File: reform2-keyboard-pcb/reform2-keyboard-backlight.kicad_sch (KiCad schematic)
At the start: 31 parts, among them J100 Conn_01x03, J5 Conn_01x03

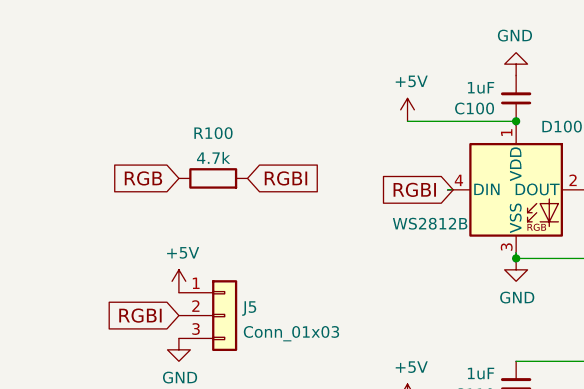
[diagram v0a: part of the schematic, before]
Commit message: more routing of smd parts, add sockets
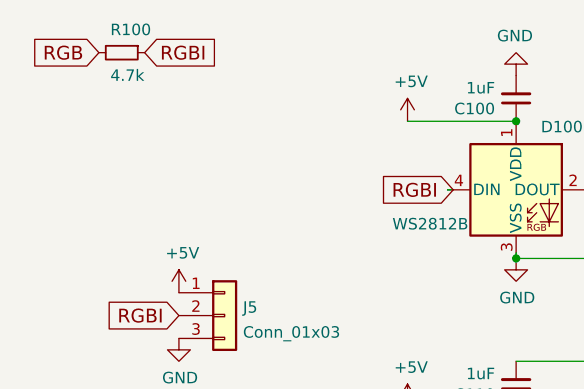
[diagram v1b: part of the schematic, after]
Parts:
- removed R100: 4.7k, Resistor_SMD:R_0603_1608Metric, symbol Device:R
- added R100: 4.7k, Resistor_SMD:R_0603_1608Metric, symbol reform2-keyboard-rescue:R_Small-Device
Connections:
- net RGB: now also R100.2
- net RGBI: now also R100.1
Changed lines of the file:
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@@
     )
   )
-  (global_label "RGBI" (shape input) (at 48.26 40.005 0) (fields_autoplaced)
+  (global_label "RGBI" (shape input) (at 36.83 26.035 0) (fields_autoplaced)
     (effects (font (size 1.524 1.524)) (justify left))
-    (property "Intersheet References" "${INTERSHEET_REFS}" (id 0) (at 56.3466 40.1002 0)
+    (property "Intersheet References" "${INTERSHEET_REFS}" (id 0) (at 44.9166 26.1302 0)
       (effects (font (size 1.524 1.524)) (justify left) hide)
     )
@@
     )
   )
-  (global_label "RGB" (shape input) (at 40.64 40.005 180) (fields_autoplaced)
+  (global_label "RGB" (shape input) (at 31.75 26.035 180) (fields_autoplaced)
     (effects (font (size 1.524 1.524)) (justify right))
-    (property "Intersheet References" "${INTERSHEET_REFS}" (id 0) (at 33.2791 39.9098 0)
+    (property "Intersheet References" "${INTERSHEET_REFS}" (id 0) (at 24.3891 25.9398 0)
       (effects (font (size 1.524 1.524)) (justify right) hide)
     )
@@
     (pin "1")
   )
+  (symbol (lib_id "reform2-keyboard-rescue:R_Small-Device") (at 34.29 26.035 270) (unit 1)
+    (in_bom yes) (on_board yes)
+    (property "Reference" "R100" (id 0) (at 33.02 23.495 90)
+      (effects (font (size 1.27 1.27)) (justify left))
+    )
+    (property "Value" "4.7k" (id 1) (at 33.02 28.575 90)
+      (effects (font (size 1.27 1.27)) (justify left))
+    )
+    (property "Footprint" "Resistor_SMD:R_0603_1608Metric" (id 2) (at 34.29 26.035 0)
+      (effects (font (size 1.27 1.27)) hide)
+    )
+    (property "Datasheet" "" (id 3) (at 34.29 26.035 0)
+      (effects (font (size 1.27 1.27)) hide)
+    )
+    (property "Manufacturer" "Vishay Dale" (id 4) (at 34.29 26.035 0)
+      (effects (font (size 1.27 1.27)) hide)
+    )
+    (property "Manufacturer_No" "CRCW06030000Z0EAC" (id 5) (at 34.29 26.035 0)
+      (effects (font (size 1.27 1.27)) hide)
+    )
+    (pin "1")
+    (pin "2")
+  )
   (symbol (lib_id "power:GND") (at 198.755 80.645 0) (unit 1)
     (in_bom yes) (on_board yes)
@@
     (pin "1")
   )
-  (symbol (lib_id "Device:R") (at 44.45 40.005 90) (unit 1)
-    (in_bom yes) (on_board yes) (fields_autoplaced)
-    (property "Reference" "R100" (id 0) (at 44.45 35.0225 90))
-    (property "Value" "4.7k" (id 1) (at 44.45 37.7976 90))
-    (property "Footprint" "Resistor_SMD:R_0603_1608Metric" (id 2) (at 44.45 41.783 90)
-      (effects (font (size 1.27 1.27)) hide)
-    )
-    (property "Datasheet" "~" (id 3) (at 44.45 40.005 0)
-      (effects (font (size 1.27 1.27)) hide)
-    )
-    (pin "1")
-    (pin "2")
-  )
   (symbol (lib_id "reform2-keyboard-rescue:C_Small-Device") (at 150.495 31.115 180) (unit 1)

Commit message: change parts for better handsolders
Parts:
- R100: footprint Resistor_SMD:R_0603_1608Metric -> Resistor_SMD:R_0805_2012Metric_Pad1.20x1.40mm_HandSolder
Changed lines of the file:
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@@
       (effects (font (size 1.27 1.27)) (justify left))
     )
-    (property "Footprint" "Resistor_SMD:R_0603_1608Metric" (id 2) (at 34.29 26.035 0)
+    (property "Footprint" "Resistor_SMD:R_0805_2012Metric_Pad1.20x1.40mm_HandSolder" (id 2) (at 34.29 26.035 0)
       (effects (font (size 1.27 1.27)) hide)
     )

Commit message: flip caps for RGB leds
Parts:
- C100, C101, C102, C103, C104, C105, C106, C110, C111, C112, C113, C114, C115, C116: footprint Capacitor_SMD:C_0603_1608Metric -> Capacitor_SMD:C_0805_2012Metric_Pad1.18x1.45mm_HandSolder
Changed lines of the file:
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@@
       (effects (font (size 1.27 1.27)) (justify left))
     )
-    (property "Footprint" "Capacitor_SMD:C_0603_1608Metric" (id 2) (at 78.105 31.115 0)
+    (property "Footprint" "Capacitor_SMD:C_0805_2012Metric_Pad1.18x1.45mm_HandSolder" (id 2) (at 78.105 31.115 0)
       (effects (font (size 1.27 1.27)) hide)
     )
@@
       (effects (font (size 1.27 1.27)) (justify left))
     )
-    (property "Footprint" "Capacitor_SMD:C_0603_1608Metric" (id 2) (at 150.495 62.865 0)
+    (property "Footprint" "Capacitor_SMD:C_0805_2012Metric_Pad1.18x1.45mm_HandSolder" (id 2) (at 150.495 62.865 0)
       (effects (font (size 1.27 1.27)) hide)
     )
@@
       (effects (font (size 1.27 1.27)) (justify left))
     )
-    (property "Footprint" "Capacitor_SMD:C_0603_1608Metric" (id 2) (at 222.885 31.115 0)
+    (property "Footprint" "Capacitor_SMD:C_0805_2012Metric_Pad1.18x1.45mm_HandSolder" (id 2) (at 222.885 31.115 0)
       (effects (font (size 1.27 1.27)) hide)
     )
@@
       (effects (font (size 1.27 1.27)) (justify left))
     )
-    (property "Footprint" "Capacitor_SMD:C_0603_1608Metric" (id 2) (at 174.625 62.865 0)
+    (property "Footprint" "Capacitor_SMD:C_0805_2012Metric_Pad1.18x1.45mm_HandSolder" (id 2) (at 174.625 62.865 0)
       (effects (font (size 1.27 1.27)) hide)
     )
@@
       (effects (font (size 1.27 1.27)) (justify left))
     )
-    (property "Footprint" "Capacitor_SMD:C_0603_1608Metric" (id 2) (at 102.235 31.115 0)
+    (property "Footprint" "Capacitor_SMD:C_0805_2012Metric_Pad1.18x1.45mm_HandSolder" (id 2) (at 102.235 31.115 0)
       (effects (font (size 1.27 1.27)) hide)
     )
@@
       (effects (font (size 1.27 1.27)) (justify left))
     )
-    (property "Footprint" "Capacitor_SMD:C_0603_1608Metric" (id 2) (at 198.755 62.865 0)
+    (property "Footprint" "Capacitor_SMD:C_0805_2012Metric_Pad1.18x1.45mm_HandSolder" (id 2) (at 198.755 62.865 0)
       (effects (font (size 1.27 1.27)) hide)
     )
@@
       (effects (font (size 1.27 1.27)) (justify left))
     )
-    (property "Footprint" "Capacitor_SMD:C_0603_1608Metric" (id 2) (at 78.105 62.865 0)
+    (property "Footprint" "Capacitor_SMD:C_0805_2012Metric_Pad1.18x1.45mm_HandSolder" (id 2) (at 78.105 62.865 0)
       (effects (font (size 1.27 1.27)) hide)
     )
@@
       (effects (font (size 1.27 1.27)) (justify left))
     )
-    (property "Footprint" "Capacitor_SMD:C_0603_1608Metric" (id 2) (at 174.625 31.115 0)
+    (property "Footprint" "Capacitor_SMD:C_0805_2012Metric_Pad1.18x1.45mm_HandSolder" (id 2) (at 174.625 31.115 0)
       (effects (font (size 1.27 1.27)) hide)
     )
@@
       (effects (font (size 1.27 1.27)) (justify left))
     )
-    (property "Footprint" "Capacitor_SMD:C_0603_1608Metric" (id 2) (at 222.885 62.865 0)
+    (property "Footprint" "Capacitor_SMD:C_0805_2012Metric_Pad1.18x1.45mm_HandSolder" (id 2) (at 222.885 62.865 0)
       (effects (font (size 1.27 1.27)) hide)
     )
@@
       (effects (font (size 1.27 1.27)) (justify left))
     )
-    (property "Footprint" "Capacitor_SMD:C_0603_1608Metric" (id 2) (at 150.495 31.115 0)
+    (property "Footprint" "Capacitor_SMD:C_0805_2012Metric_Pad1.18x1.45mm_HandSolder" (id 2) (at 150.495 31.115 0)
       (effects (font (size 1.27 1.27)) hide)
     )
@@
       (effects (font (size 1.27 1.27)) (justify left))
     )
-    (property "Footprint" "Capacitor_SMD:C_0603_1608Metric" (id 2) (at 198.755 31.115 0)
+    (property "Footprint" "Capacitor_SMD:C_0805_2012Metric_Pad1.18x1.45mm_HandSolder" (id 2) (at 198.755 31.115 0)
       (effects (font (size 1.27 1.27)) hide)
     )
@@
       (effects (font (size 1.27 1.27)) (justify left))
     )
-    (property "Footprint" "Capacitor_SMD:C_0603_1608Metric" (id 2) (at 126.365 31.115 0)
+    (property "Footprint" "Capacitor_SMD:C_0805_2012Metric_Pad1.18x1.45mm_HandSolder" (id 2) (at 126.365 31.115 0)
       (effects (font (size 1.27 1.27)) hide)
     )
@@
       (effects (font (size 1.27 1.27)) (justify left))
     )
-    (property "Footprint" "Capacitor_SMD:C_0603_1608Metric" (id 2) (at 102.235 62.865 0)
+    (property "Footprint" "Capacitor_SMD:C_0805_2012Metric_Pad1.18x1.45mm_HandSolder" (id 2) (at 102.235 62.865 0)
       (effects (font (size 1.27 1.27)) hide)
     )
@@
       (effects (font (size 1.27 1.27)) (justify left))
     )
-    (property "Footprint" "Capacitor_SMD:C_0603_1608Metric" (id 2) (at 126.365 62.865 0)
-      (effects (font (size 1.27 1.27)) hide)
-    )
+    (property "Footprint" "Capacitor_SMD:C_0805_2012Metric_Pad1.18x1.45mm_HandSolder" (id 2) (at 126.365 62.865 0)
+      (effects (font (size 1.27 1.27)) hide)
+    )

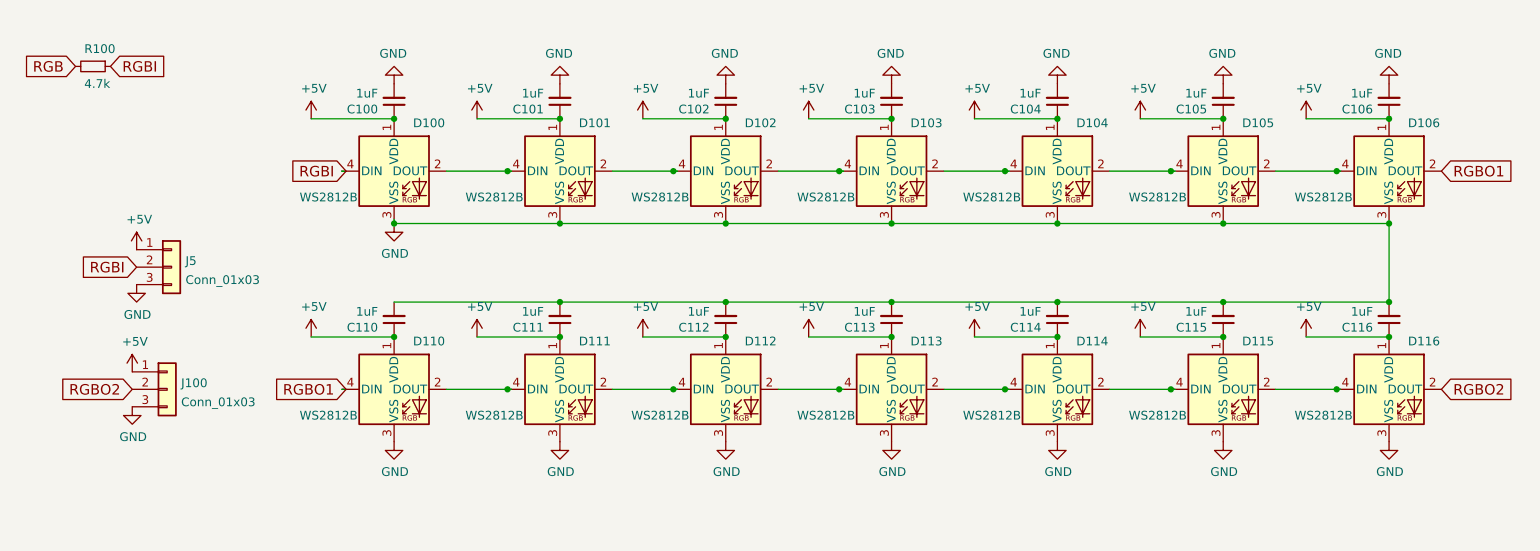
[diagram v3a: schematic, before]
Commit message: added testpoints for RGB, fixed diode directions, started BOM & top POS for assembly
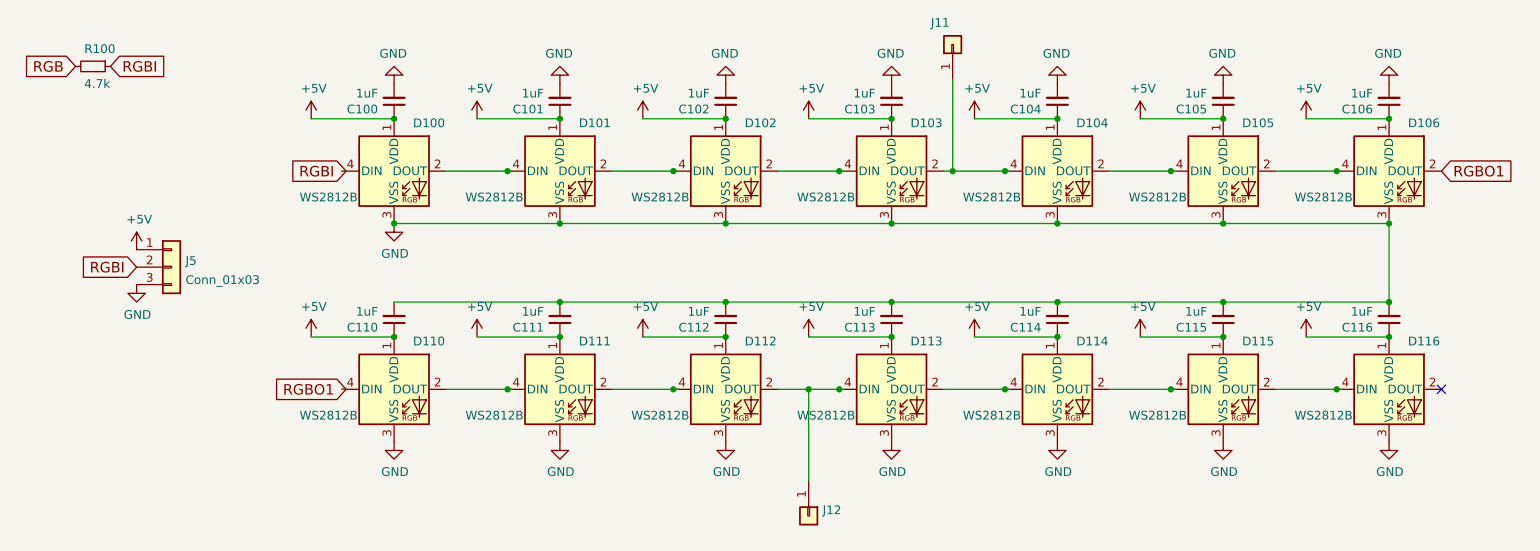
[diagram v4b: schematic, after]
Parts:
- removed J100: Conn_01x03, Connector_PinHeader_2.54mm:PinHeader_1x03_P2.54mm_Vertical, symbol Connector_Generic:Conn_01x03
- added J11, J12: (no value), symbol Connector_Generic:Conn_01x01
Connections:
- net at D103.2 (DOUT), D104.4 (DIN): now also J11.1 (Pin_1)
- net at D112.2 (DOUT), D113.4 (DIN): now also J12.1 (Pin_1)
- net RGBO2: no longer names the net of D116.2 (DOUT)
- no-connect marks 0 -> 1
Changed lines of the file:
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@@
   (junction (at 198.755 60.325) (diameter 0) (color 0 0 0 0)
   )
+  (junction (at 138.43 73.025) (diameter 0) (color 0 0 0 0)
+  )
   (junction (at 150.495 60.325) (diameter 0) (color 0 0 0 0)
   )
   (junction (at 94.615 73.025) (diameter 0) (color 0 0 0 0)
   )
+  (junction (at 159.385 41.275) (diameter 0) (color 0 0 0 0)
+  )
   (junction (at 150.495 48.895) (diameter 0) (color 0 0 0 0)
   )
@@
   (junction (at 198.755 33.655) (diameter 0) (color 0 0 0 0)
   )
+  (no_connect (at 230.505 73.025))
   (wire (pts (xy 198.755 60.325) (xy 222.885 60.325))
     (stroke (width 0) (type default) (color 0 0 0 0))
@@
     (stroke (width 0) (type default) (color 0 0 0 0))
   )
-  (wire (pts (xy 158.115 41.275) (xy 167.005 41.275))
+  (wire (pts (xy 158.115 41.275) (xy 159.385 41.275))
     (stroke (width 0) (type default) (color 0 0 0 0))
   )
@@
     (stroke (width 0) (type default) (color 0 0 0 0))
   )
+  (wire (pts (xy 159.385 41.275) (xy 167.005 41.275))
+    (stroke (width 0) (type default) (color 0 0 0 0))
+  )
   (wire (pts (xy 102.235 48.895) (xy 78.105 48.895))
     (stroke (width 0) (type default) (color 0 0 0 0))
@@
     (stroke (width 0) (type default) (color 0 0 0 0))
   )
-  (wire (pts (xy 133.985 73.025) (xy 142.875 73.025))
+  (wire (pts (xy 133.985 73.025) (xy 138.43 73.025))
     (stroke (width 0) (type default) (color 0 0 0 0))
   )
@@
     (stroke (width 0) (type default) (color 0 0 0 0))
   )
+  (wire (pts (xy 138.43 73.025) (xy 142.875 73.025))
+    (stroke (width 0) (type default) (color 0 0 0 0))
+  )
   (wire (pts (xy 206.375 41.275) (xy 215.265 41.275))
     (stroke (width 0) (type default) (color 0 0 0 0))
@@
     (stroke (width 0) (type default) (color 0 0 0 0))
   )
+  (wire (pts (xy 138.43 86.36) (xy 138.43 73.025))
+    (stroke (width 0) (type default) (color 0 0 0 0))
+  )
   (wire (pts (xy 162.56 33.655) (xy 174.625 33.655))
     (stroke (width 0) (type default) (color 0 0 0 0))
@@
   )
   (wire (pts (xy 186.69 33.655) (xy 198.755 33.655))
+    (stroke (width 0) (type default) (color 0 0 0 0))
+  )
+  (wire (pts (xy 159.385 27.94) (xy 159.385 41.275))
     (stroke (width 0) (type default) (color 0 0 0 0))
   )
@@
     )
   )
-  (global_label "RGBO2" (shape input) (at 230.505 73.025 0) (fields_autoplaced)
-    (effects (font (size 1.524 1.524)) (justify left))
-    (property "Intersheet References" "${INTERSHEET_REFS}" (id 0) (at 240.9139 72.9298 0)
-      (effects (font (size 1.524 1.524)) (justify left) hide)
-    )
-  )
-  (global_label "RGBO2" (shape input) (at 40.005 73.025 180) (fields_autoplaced)
-    (effects (font (size 1.524 1.524)) (justify right))
-    (property "Intersheet References" "${INTERSHEET_REFS}" (id 0) (at 29.5961 72.9298 0)
-      (effects (font (size 1.524 1.524)) (justify right) hide)
-    )
-  )
   (global_label "RGB" (shape input) (at 31.75 26.035 180) (fields_autoplaced)
     (effects (font (size 1.524 1.524)) (justify right))
@@
     (pin "1")
   )
-  (symbol (lib_id "power:GND") (at 40.005 75.565 0) (unit 1)
-    (in_bom yes) (on_board yes)
-    (property "Reference" "#PWR0112" (id 0) (at 40.005 81.915 0)
-      (effects (font (size 1.27 1.27)) hide)
-    )
-    (property "Value" "GND" (id 1) (at 40.132 79.9592 0))
-    (property "Footprint" "" (id 2) (at 40.005 75.565 0)
-      (effects (font (size 1.27 1.27)) hide)
-    )
-    (property "Datasheet" "" (id 3) (at 40.005 75.565 0)
+  (symbol (lib_id "Connector_Generic:Conn_01x01") (at 159.385 22.86 90) (unit 1)
+    (in_bom yes) (on_board yes)
+    (property "Reference" "J11" (id 0) (at 156.21 19.685 90)
+      (effects (font (size 1.27 1.27)) (justify right))
+    )
+    (property "Value" "" (id 1) (at 160.655 19.685 90)
+      (effects (font (size 1.27 1.27)) (justify right))
+    )
+    (property "Footprint" "" (id 2) (at 159.385 22.86 0)
+      (effects (font (size 1.27 1.27)) hide)
+    )
+    (property "Datasheet" "~" (id 3) (at 159.385 22.86 0)
       (effects (font (size 1.27 1.27)) hide)
     )
@@
     (pin "1")
   )
-  (symbol (lib_id "Connector_Generic:Conn_01x03") (at 45.085 73.025 0) (unit 1)
-    (in_bom yes) (on_board yes) (fields_autoplaced)
-    (property "Reference" "J100" (id 0) (at 47.117 72.1165 0)
-      (effects (font (size 1.27 1.27)) (justify left))
-    )
-    (property "Value" "Conn_01x03" (id 1) (at 47.117 74.8916 0)
-      (effects (font (size 1.27 1.27)) (justify left))
-    )
-    (property "Footprint" "Connector_PinHeader_2.54mm:PinHeader_1x03_P2.54mm_Vertical" (id 2) (at 45.085 73.025 0)
-      (effects (font (size 1.27 1.27)) hide)
-    )
-    (property "Datasheet" "~" (id 3) (at 45.085 73.025 0)
-      (effects (font (size 1.27 1.27)) hide)
-    )
-    (pin "1")
-    (pin "2")
-    (pin "3")
-  )
   (symbol (lib_id "power:+5V") (at 114.3 33.655 0) (unit 1)
     (in_bom yes) (on_board yes)
@@
     (pin "4")
   )
-  (symbol (lib_id "power:+5V") (at 40.005 70.485 0) (unit 1)
-    (in_bom yes) (on_board yes)
-    (property "Reference" "#PWR0111" (id 0) (at 40.005 74.295 0)
-      (effects (font (size 1.27 1.27)) hide)
-    )
-    (property "Value" "+5V" (id 1) (at 40.386 66.0908 0))
-    (property "Footprint" "" (id 2) (at 40.005 70.485 0)
-      (effects (font (size 1.27 1.27)) hide)
-    )
-    (property "Datasheet" "" (id 3) (at 40.005 70.485 0)
-      (effects (font (size 1.27 1.27)) hide)
-    )
-    (pin "1")
-  )
   (symbol (lib_id "reform2-keyboard-rescue:C_Small-Device") (at 174.625 31.115 180) (unit 1)
     (in_bom yes) (on_board yes)
@@
       (effects (font (size 1.27 1.27)) hide)
     )
+    (pin "1")
+  )
+  (symbol (lib_id "Connector_Generic:Conn_01x01") (at 138.43 91.44 270) (unit 1)
+    (in_bom yes) (on_board yes) (fields_autoplaced)
+    (property "Reference" "J12" (id 0) (at 140.462 90.6053 90)
+      (effects (font (size 1.27 1.27)) (justify left))
+    )
+    (property "Value" "" (id 1) (at 140.462 93.1422 90)
+      (effects (font (size 1.27 1.27)) (justify left))
+    )
+    (property "Footprint" "" (id 2) (at 138.43 91.44 0)
+      (effects (font (size 1.27 1.27)) hide)
+    )
+    (property "Datasheet" "~" (id 3) (at 138.43 91.44 0)
+      (effects (font (size 1.27 1.27)) hide)
+    )

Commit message: improve docs
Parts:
- J11, J12: value (none) -> Conn_01x01; footprint (none) -> Connector_PinHeader_2.00mm:PinHeader_1x01_P2.00mm_Vertical
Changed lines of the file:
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@@
       (effects (font (size 1.27 1.27)) (justify right))
     )
-    (property "Value" "" (id 1) (at 160.655 19.685 90)
+    (property "Value" "Conn_01x01" (id 1) (at 160.655 19.685 90)
       (effects (font (size 1.27 1.27)) (justify right))
     )
-    (property "Footprint" "" (id 2) (at 159.385 22.86 0)
+    (property "Footprint" "Connector_PinHeader_2.00mm:PinHeader_1x01_P2.00mm_Vertical" (id 2) (at 159.385 22.86 0)
       (effects (font (size 1.27 1.27)) hide)
     )
@@
       (effects (font (size 1.27 1.27)) (justify left))
     )
-    (property "Value" "" (id 1) (at 140.462 93.1422 90)
-      (effects (font (size 1.27 1.27)) (justify left))
-    )
-    (property "Footprint" "" (id 2) (at 138.43 91.44 0)
-      (effects (font (size 1.27 1.27)) hide)
-    )
+    (property "Value" "Conn_01x01" (id 1) (at 140.462 93.1422 90)
+      (effects (font (size 1.27 1.27)) (justify left))
+    )
+    (property "Footprint" "Connector_PinHeader_2.00mm:PinHeader_1x01_P2.00mm_Vertical" (id 2) (at 138.43 91.44 0)
+      (effects (font (size 1.27 1.27)) hide)
+    )
